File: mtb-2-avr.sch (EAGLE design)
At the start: 16 parts, among them IC1 MEGA8A-AU, Q1 14.745 MHz

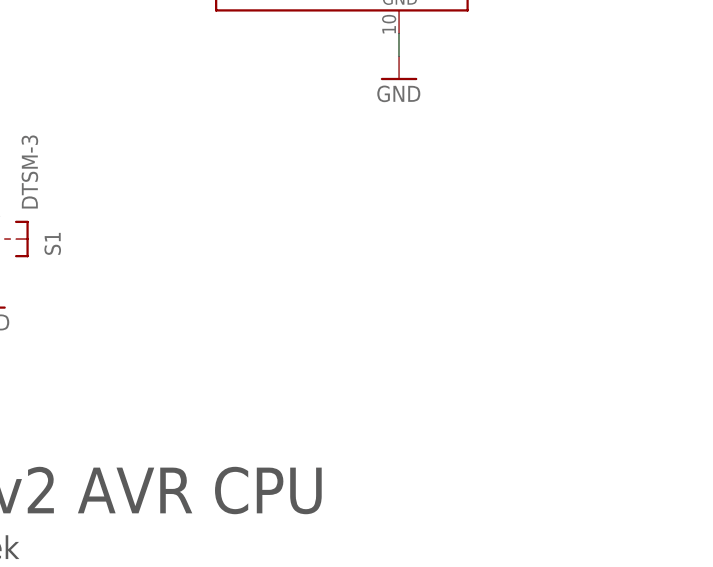
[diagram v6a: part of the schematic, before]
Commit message: Add GND testpads.
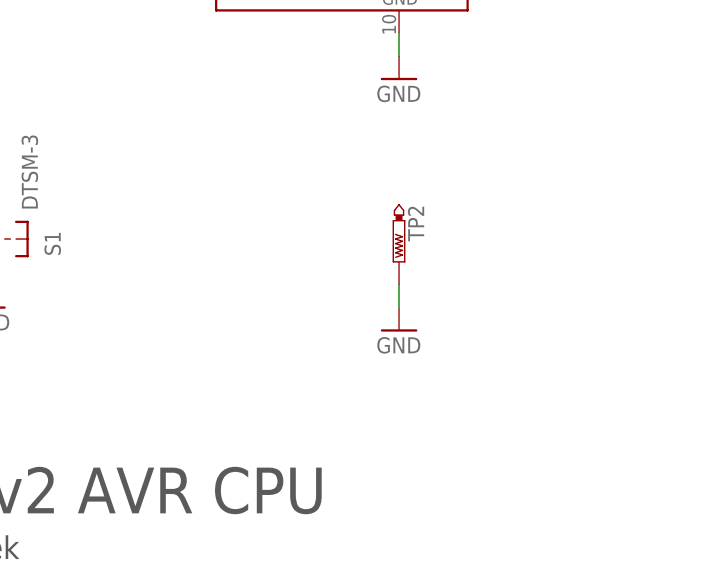
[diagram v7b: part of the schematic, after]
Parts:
- added TP2: PTR1B1,27, testpad:PTR1B1,27
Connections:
- net GND: now also TP2.TP
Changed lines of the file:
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@@
 <part name="GND4" library="supply1" library_urn="urn:adsk.eagle:library:371" deviceset="GND" device=""/>
 <part name="TP1" library="testpad" library_urn="urn:adsk.eagle:library:385" deviceset="PTR1" device="B1,27" package3d_urn="urn:adsk.eagle:package:27944/2"/>
+<part name="TP2" library="testpad" library_urn="urn:adsk.eagle:library:385" deviceset="PTR1" device="B1,27" package3d_urn="urn:adsk.eagle:package:27944/2"/>
+<part name="GND5" library="supply1" library_urn="urn:adsk.eagle:library:371" deviceset="GND" device=""/>
 </parts>
 <sheets>
@@
 <attribute name="NAME" x="95.25" y="80.264" size="1.778" layer="95" rot="R180"/>
 <attribute name="TP_SIGNAL_NAME" x="91.44" y="82.55" size="1.778" layer="97" rot="R90"/>
+</instance>
+<instance part="TP2" gate="G$1" x="147.32" y="45.72" smashed="yes" rot="R180">
+<attribute name="NAME" x="148.336" y="52.07" size="1.778" layer="95" rot="R270"/>
+<attribute name="TP_SIGNAL_NAME" x="146.05" y="48.26" size="1.778" layer="97" rot="R180"/>
+</instance>
+<instance part="GND5" gate="1" x="147.32" y="38.1" smashed="yes">
+<attribute name="VALUE" x="144.78" y="35.56" size="1.778" layer="96"/>
 </instance>
 </instances>
@@
 <pinref part="GND4" gate="1" pin="GND"/>
 </segment>
-</net>
+<segment>
+<pinref part="TP2" gate="G$1" pin="TP"/>
+<pinref part="GND5" gate="1" pin="GND"/>
+<wire x1="147.32" y1="43.18" x2="147.32" y2="40.64" width="0.1524" layer="91"/>
+</segment>
+</net>

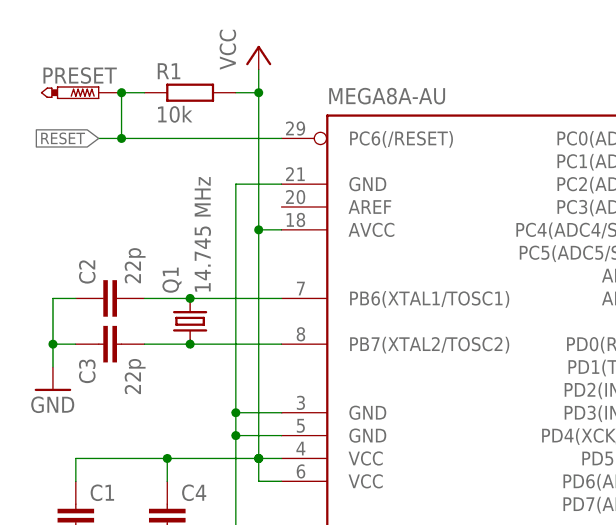
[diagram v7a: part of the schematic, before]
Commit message: Add possibility for THT crystal.
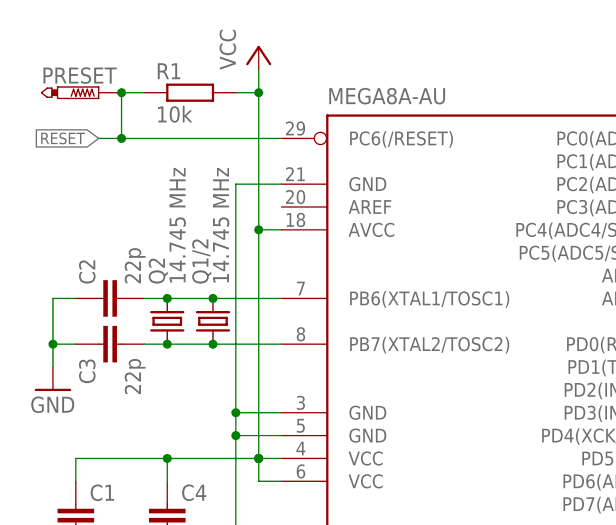
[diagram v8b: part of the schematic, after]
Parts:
- removed Q1: 14.745 MHz, crystal:CRYSTALHC49UP
- added Q1/2: 14.745 MHz, crystal:CRYSTALHC49UP
- added Q2: 14.745 MHz, crystal:CRYSTALHC49S
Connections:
- removed net N$1: C2.2, IC1.PB6(XTAL1/TOSC1), Q1.2
- removed net N$2: C3.2, IC1.PB7(XTAL2/TOSC2), Q1.1
- new net CRYST+: C2.2, IC1.PB6(XTAL1/TOSC1), Q1/2.2, Q2.2
- new net CRYST-: C3.2, IC1.PB7(XTAL2/TOSC2), Q1/2.1, Q2.1
